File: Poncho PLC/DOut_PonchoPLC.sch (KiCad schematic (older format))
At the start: 66 parts, among them J10 TB_1X3, J11 TB_1X3, J6 TB_1X2, J7 TB_1X2, J8 TB_1X3, J9 TB_1X3, K1 RELAY_C, K2 RELAY_C, K3 RELAY_C, K4 RELAY_C, Q1 FQT13N06L, Q2 FQT13N06L, Q3 FQT13N06L, Q4 FQT13N06L, Q5 2N7002, Q6 2N7002, Q7 2N7002, Q8 2N7002, U3 MCP1416, U4 MCP1416, U5 MCP1416, U6 MCP1416

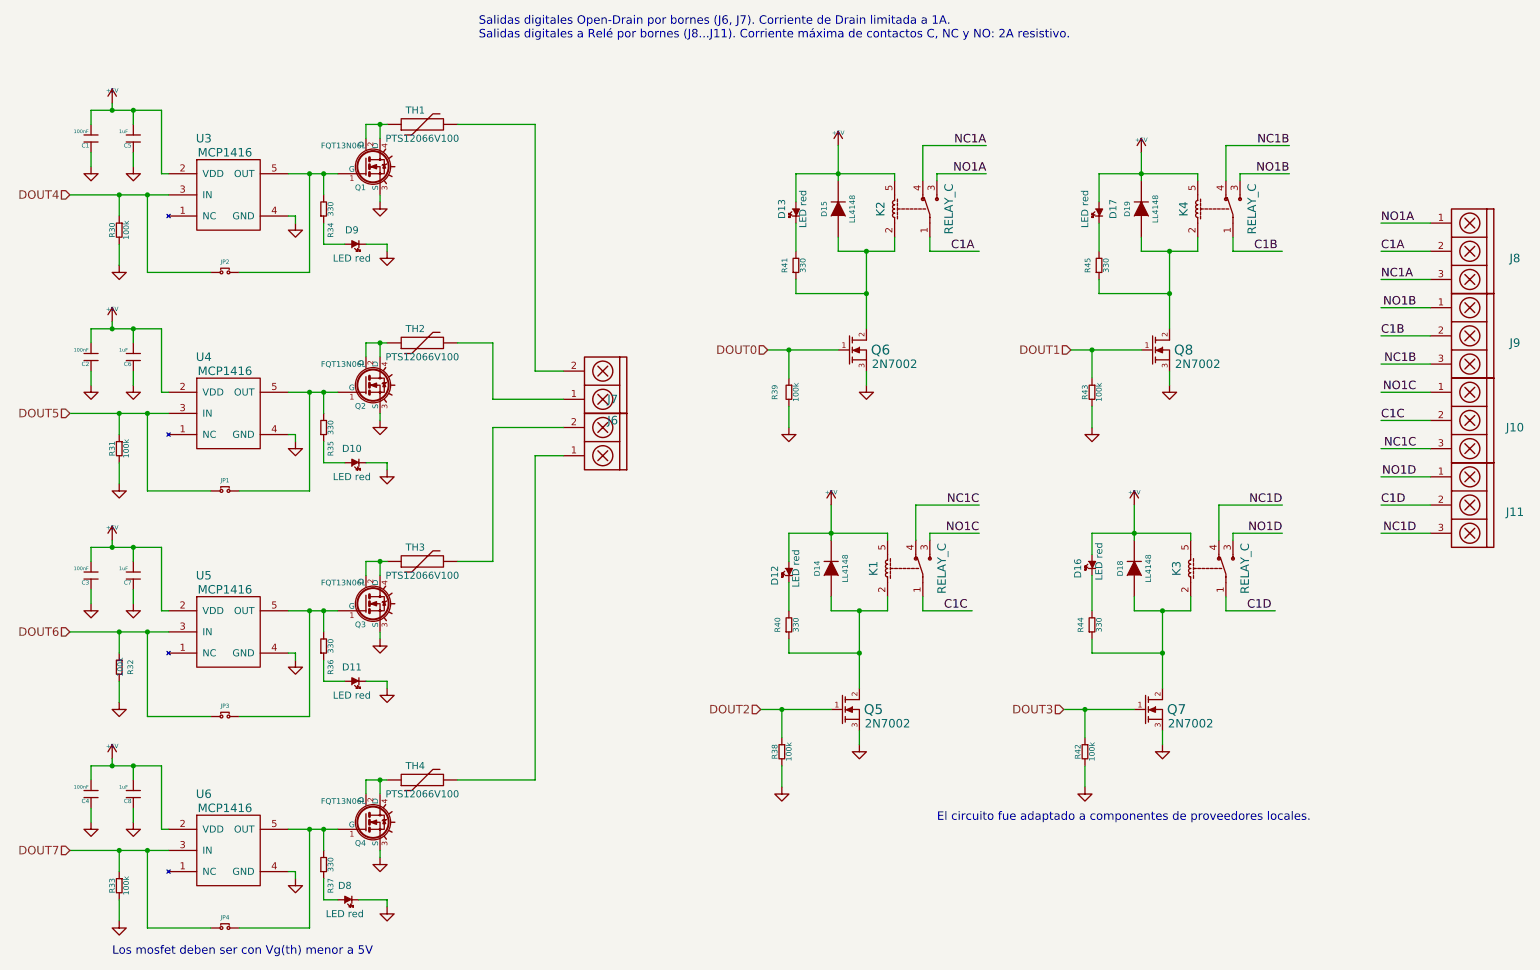
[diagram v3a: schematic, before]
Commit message: Avance posicionamiento
Se avanzo en el posicionamiento de componentes.
Se actualizo el modelo 3D de varios componentes.
Se agregaron los logos de la escuela y de Open Hardware.
Falta actualizar las librerias del repositorio y las rutas relativas de
los modelos 3D para que la vista 3D sea portable a cualquier pc.
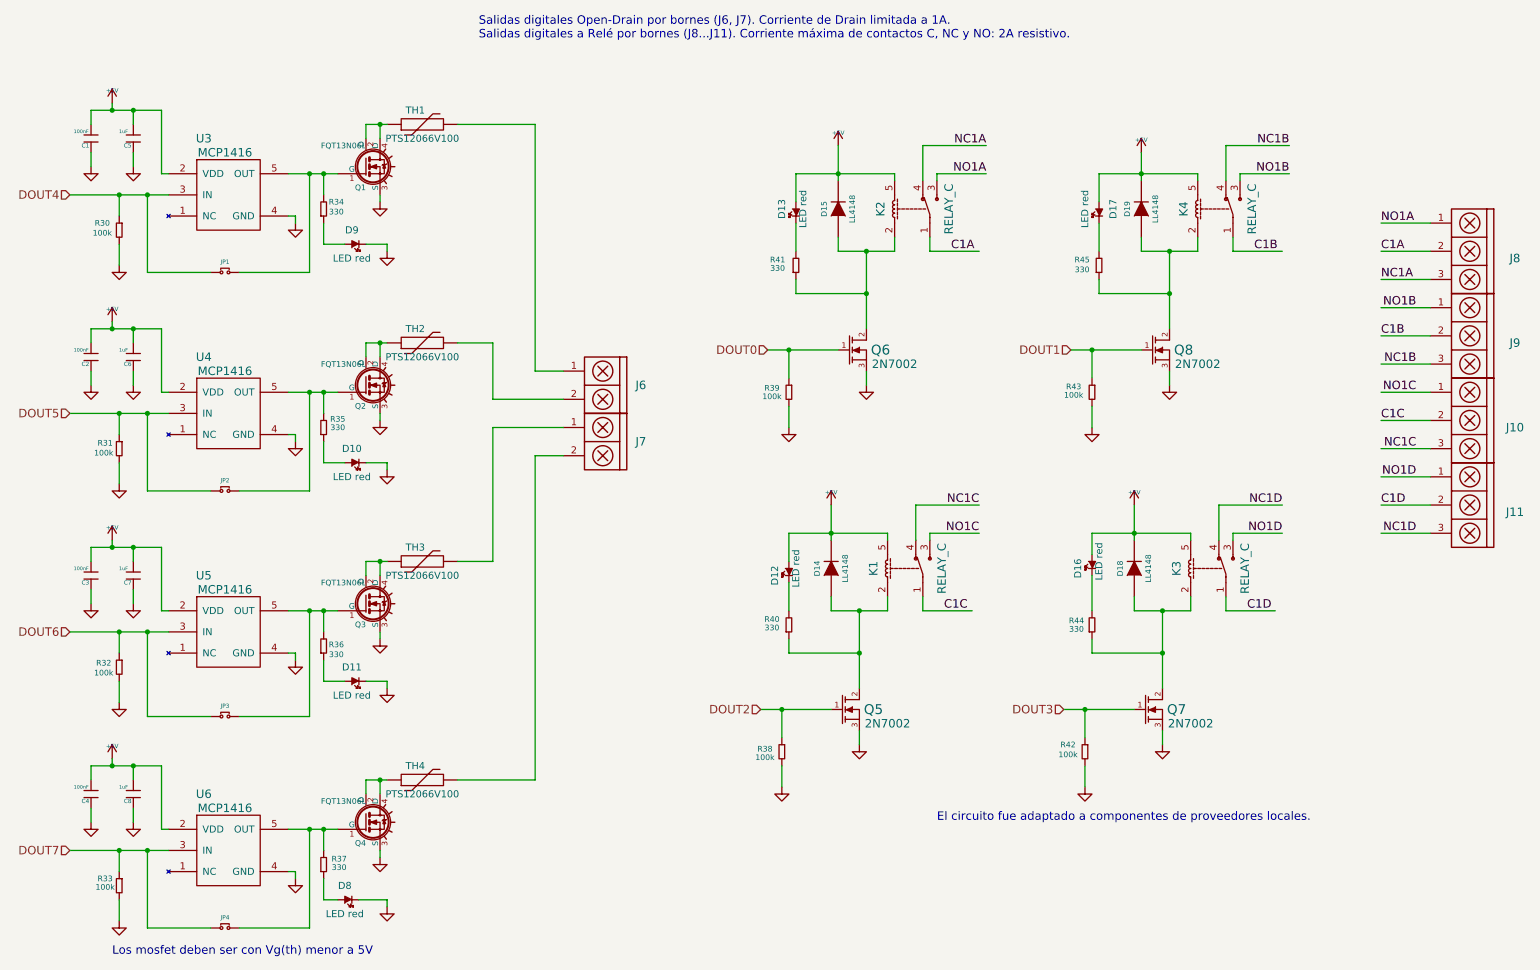
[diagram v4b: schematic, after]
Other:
- moved on the sheet: JP1, JP2
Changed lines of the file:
@@
 U 1 1 52CA436C
 P 5950 3450
-F 0 "R39" V 5850 3450 40  0000 C CNN
-F 1 "100k" V 6000 3450 40  0000 C CNN
+F 0 "R39" H 5830 3480 40  0000 C CNN
+F 1 "100k" H 5830 3420 40  0000 C CNN
 F 2 "Poncho-PLC:R_1206" V 5880 3450 30  0001 C CNN
 F 3 "~" H 5950 3450 30  0000 C CNN
@@
 U 1 1 52CA48D5
 P 1200 2300
-F 0 "R30" V 1150 2300 40  0000 C CNN
-F 1 "100k" V 1250 2300 40  0000 C CNN
+F 0 "R30" H 1080 2350 40  0000 C CNN
+F 1 "100k" H 1080 2280 40  0000 C CNN
 F 2 "Poncho-PLC:R_1206" V 1130 2300 30  0001 C CNN
 F 3 "~" H 1200 2300 30  0000 C CNN
@@
 U 1 1 52E0878B
 P 2650 2150
-F 0 "R34" V 2600 2300 40  0000 C CNN
-F 1 "330" V 2600 2150 40  0000 C CNN
+F 0 "R34" H 2560 2100 40  0000 C CNN
+F 1 "330" H 2560 2170 40  0000 C CNN
 F 2 "Poncho-PLC:R_1206" V 2580 2150 30  0001 C CNN
 F 3 "~" H 2650 2150 30  0000 C CNN
@@
 U 1 1 52E032C2
 P 6000 2550
-F 0 "R41" V 6080 2550 40  0000 C CNN
-F 1 "330" V 5950 2550 40  0000 C CNN
+F 0 "R41" H 6130 2510 40  0000 C CNN
+F 1 "330" H 6130 2570 40  0000 C CNN
 F 2 "Poncho-PLC:R_1206" V 5930 2550 30  0001 C CNN
 F 3 "~" H 6000 2550 30  0000 C CNN
@@
 U 1 1 56D4FD3E
 P 5900 6000
-F 0 "R38" V 5850 6000 40  0000 C CNN
-F 1 "100k" V 5950 6000 40  0000 C CNN
+F 0 "R38" H 5780 6020 40  0000 C CNN
+F 1 "100k" H 5780 5960 40  0000 C CNN
 F 2 "Poncho-PLC:R_1206" V 5830 6000 30  0001 C CNN
 F 3 "~" H 5900 6000 30  0000 C CNN
@@
 U 1 1 56D4FD49
 P 5950 5100
-F 0 "R40" V 6030 5100 40  0000 C CNN
-F 1 "330" V 5900 5100 40  0000 C CNN
+F 0 "R40" H 6070 5060 40  0000 C CNN
+F 1 "330" H 6070 5120 40  0000 C CNN
 F 2 "Poncho-PLC:R_1206" V 5880 5100 30  0001 C CNN
 F 3 "~" H 5950 5100 30  0000 C CNN
@@
 U 1 1 56D503E7
 P 8100 3450
-F 0 "R43" V 8050 3450 40  0000 C CNN
-F 1 "100k" V 8150 3450 40  0000 C CNN
+F 0 "R43" H 7970 3490 40  0000 C CNN
+F 1 "100k" H 7970 3430 40  0000 C CNN
 F 2 "Poncho-PLC:R_1206" V 8030 3450 30  0001 C CNN
 F 3 "~" H 8100 3450 30  0000 C CNN
@@
 U 1 1 56D503F2
 P 8150 2550
-F 0 "R45" V 8230 2550 40  0000 C CNN
-F 1 "330" V 8100 2550 40  0000 C CNN
+F 0 "R45" H 8270 2510 40  0000 C CNN
+F 1 "330" H 8270 2580 40  0000 C CNN
 F 2 "Poncho-PLC:R_1206" V 8080 2550 30  0001 C CNN
 F 3 "~" H 8150 2550 30  0000 C CNN
@@
 U 1 1 56D5043C
 P 8050 6000
-F 0 "R42" V 8000 6000 40  0000 C CNN
-F 1 "100k" V 8100 6000 40  0000 C CNN
+F 0 "R42" H 7930 6050 40  0000 C CNN
+F 1 "100k" H 7930 5980 40  0000 C CNN
 F 2 "Poncho-PLC:R_1206" V 7980 6000 30  0001 C CNN
 F 3 "~" H 8050 6000 30  0000 C CNN
@@
 U 1 1 56D50447
 P 8100 5100
-F 0 "R44" V 8180 5100 40  0000 C CNN
-F 1 "330" V 8050 5100 40  0000 C CNN
+F 0 "R44" H 8210 5070 40  0000 C CNN
+F 1 "330" H 8210 5130 40  0000 C CNN
 F 2 "Poncho-PLC:R_1206" V 8030 5100 30  0001 C CNN
 F 3 "~" H 8100 5100 30  0000 C CNN
@@
 U 1 1 56D3641A
 P 1200 3850
-F 0 "R31" V 1150 3850 40  0000 C CNN
-F 1 "100k" V 1250 3850 40  0000 C CNN
+F 0 "R31" H 1100 3890 40  0000 C CNN
+F 1 "100k" H 1090 3820 40  0000 C CNN
 F 2 "Poncho-PLC:R_1206" V 1130 3850 30  0001 C CNN
 F 3 "~" H 1200 3850 30  0000 C CNN
@@
 U 1 1 56D3642F
 P 2650 3700
-F 0 "R35" V 2600 3850 40  0000 C CNN
-F 1 "330" V 2600 3700 40  0000 C CNN
+F 0 "R35" H 2550 3640 40  0000 C CNN
+F 1 "330" H 2550 3700 40  0000 C CNN
 F 2 "Poncho-PLC:R_1206" V 2580 3700 30  0001 C CNN
 F 3 "~" H 2650 3700 30  0000 C CNN
@@
 U 1 1 56D36B00
 P 1200 5400
-F 0 "R32" V 1280 5400 40  0000 C CNN
-F 1 "100k" V 1207 5401 40  0000 C CNN
+F 0 "R32" H 1090 5430 40  0000 C CNN
+F 1 "100k" H 1090 5360 40  0000 C CNN
 F 2 "Poncho-PLC:R_1206" V 1130 5400 30  0001 C CNN
 F 3 "~" H 1200 5400 30  0000 C CNN
@@
 U 1 1 56D36B15
 P 2650 5250
-F 0 "R36" V 2600 5400 40  0000 C CNN
-F 1 "330" V 2600 5250 40  0000 C CNN
+F 0 "R36" H 2560 5240 40  0000 C CNN
+F 1 "330" H 2560 5310 40  0000 C CNN
 F 2 "Poncho-PLC:R_1206" V 2580 5250 30  0001 C CNN
 F 3 "~" H 2650 5250 30  0000 C CNN
@@
 U 1 1 56D36B7F
 P 1200 6950
-F 0 "R33" V 1150 6950 40  0000 C CNN
-F 1 "100k" V 1250 6950 40  0000 C CNN
+F 0 "R33" H 1100 7000 40  0000 C CNN
+F 1 "100k" H 1100 6940 40  0000 C CNN
 F 2 "Poncho-PLC:R_1206" V 1130 6950 30  0001 C CNN
 F 3 "~" H 1200 6950 30  0000 C CNN
@@
 U 1 1 56D36B94
 P 2650 6800
-F 0 "R37" V 2600 6950 40  0000 C CNN
-F 1 "330" V 2600 6800 40  0000 C CNN
+F 0 "R37" H 2540 6760 40  0000 C CNN
+F 1 "330" H 2540 6820 40  0000 C CNN
 F 2 "Poncho-PLC:R_1206" V 2580 6800 30  0001 C CNN
 F 3 "~" H 2650 6800 30  0000 C CNN
@@
 U 1 1 56D45CFD
 P 4700 3400
-F 0 "J6" H 4700 3650 60  0000 C CNN
+F 0 "J6" H 4500 3400 60  0000 C CNN
 F 1 "TB_1X2" H 4750 3100 60  0001 C CNN
 F 2 "Poncho-PLC:BORNERA2" H 4650 3450 60  0001 C CNN
@@
 F 4 "Esqueleto EDU-CIAA" H 4700 3400 60  0001 C CNN "Title"
 	1    4700 3400
-	-1   0    0    1
+	-1   0    0    -1
 $EndComp
 $Comp
@@
 U 1 1 56D45E9C
 P 4700 3800
-F 0 "J7" H 4700 3500 60  0000 C CNN
+F 0 "J7" H 4500 3800 60  0000 C CNN
 F 1 "TB_1X2" H 4750 3500 60  0001 C CNN
 F 2 "Poncho-PLC:BORNERA2" H 4650 3850 60  0001 C CNN
@@
 F 4 "Esqueleto EDU-CIAA" H 4700 3800 60  0001 C CNN "Title"
 	1    4700 3800
-	-1   0    0    1
+	-1   0    0    -1
 $EndComp
 Text Notes 1150 7450 0    60   ~ 0
@@
 L Jumper JP2
 U 1 1 56DDC953
+P 1950 4150
+F 0 "JP2" H 1950 4075 30  0000 C CNN
+F 1 "Jumper" H 1950 4200 30  0001 C CNN
+F 2 "Poncho-PLC:Pin_strip_2" H 1950 4150 60  0001 C CNN
+F 3 "" H 1950 4150 60  0000 C CNN
+F 4 "Esqueleto EDU-CIAA" H 1950 4150 60  0001 C CNN "Title"
+	1    1950 4150
+	1    0    0    1
+$EndComp
+$Comp
+L Jumper JP1
+U 1 1 56DE30B8
 P 1950 2600
-F 0 "JP2" H 1950 2525 30  0000 C CNN
+F 0 "JP1" H 1950 2525 30  0000 C CNN
 F 1 "Jumper" H 1950 2650 30  0001 C CNN
 F 2 "Poncho-PLC:Pin_strip_2" H 1950 2600 60  0001 C CNN
@@
 	1    0    0    1
 $EndComp
-$Comp
-L Jumper JP1
-U 1 1 56DE30B8
-P 1950 4150
-F 0 "JP1" H 1950 4075 30  0000 C CNN
-F 1 "Jumper" H 1950 4200 30  0001 C CNN
-F 2 "Poncho-PLC:Pin_strip_2" H 1950 4150 60  0001 C CNN
-F 3 "" H 1950 4150 60  0000 C CNN
-F 4 "Esqueleto EDU-CIAA" H 1950 4150 60  0001 C CNN "Title"
-	1    1950 4150
-	1    0    0    1
-$EndComp

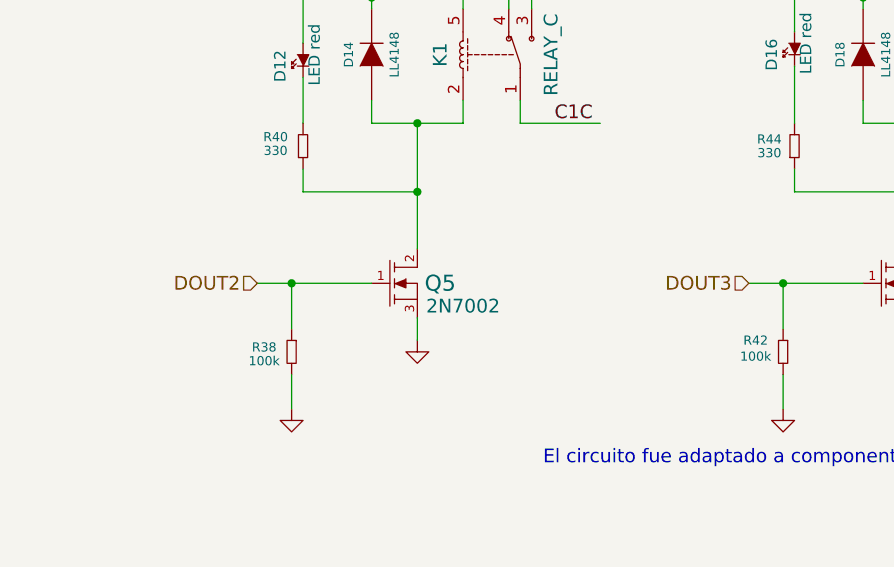
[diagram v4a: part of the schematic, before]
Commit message: Avances varios
Se avanzo en el routeo de la placa, solo quedan 7 conexiones.
Se incluyo el logo del proyecto CIAA.
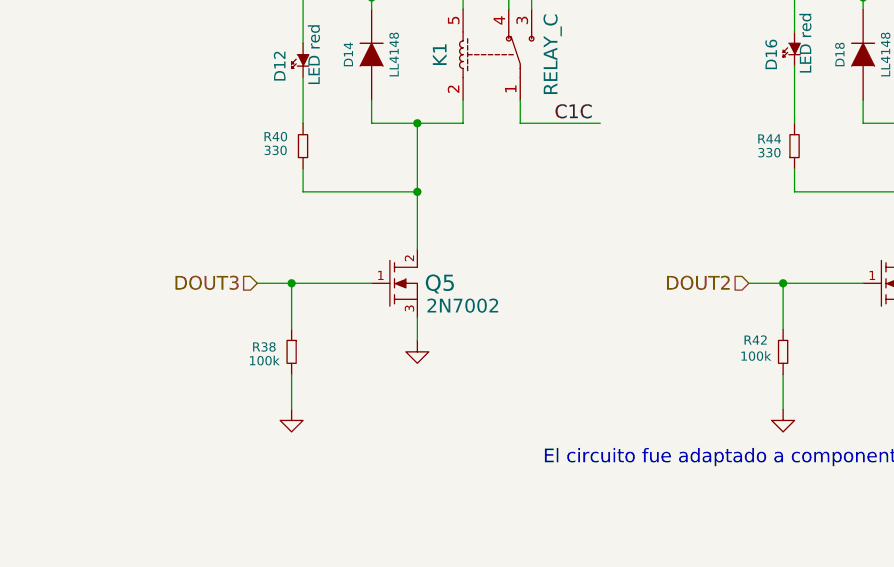
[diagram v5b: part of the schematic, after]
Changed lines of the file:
@@
 	1    0    0    -1
 $EndComp
-Text HLabel 5750 5700 0    60   Input ~ 0
+Text HLabel 7900 5700 0    60   Input ~ 0
 DOUT2
 Text Label 7050 5000 0    60   ~ 0
@@
 	1    0    0    -1
 $EndComp
-Text HLabel 7900 5700 0    60   Input ~ 0
+Text HLabel 5750 5700 0    60   Input ~ 0
 DOUT3
 Text Label 9200 5000 0    60   ~ 0
